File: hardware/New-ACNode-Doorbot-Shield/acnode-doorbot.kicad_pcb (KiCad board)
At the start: 2 copper layers, 55.9 x 124.5 mm, 19 parts, among them J1 Conn_02x10_Odd_Even, J10 Screw_Terminal_01x03, J2 Conn_02x10_Odd_Even, J3 Screw_Terminal_01x02, J4 Conn_02x10_Odd_Even, J5 Conn_02x10_Odd_Even, J6 Screw_Terminal_01x02, J7 Screw_Terminal_01x03, J8 RJ45, J9 Micro_SD_Card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

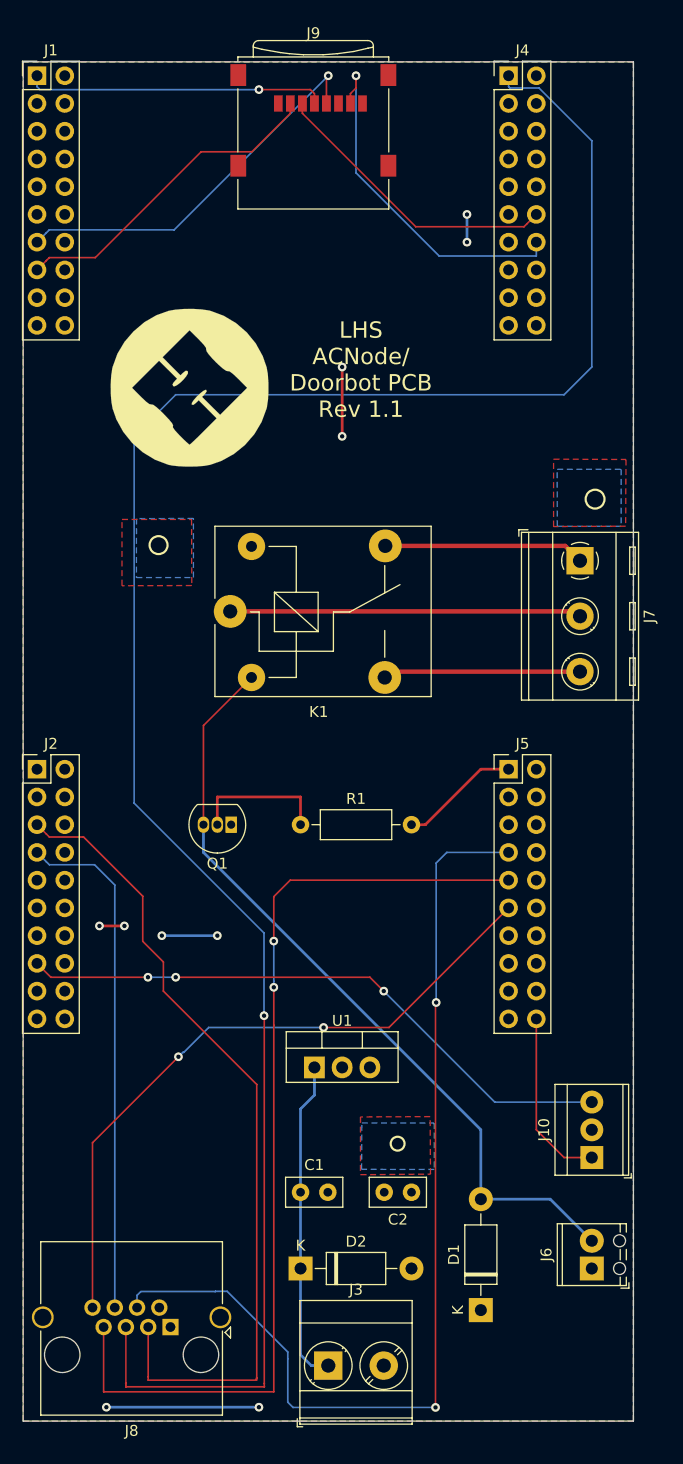
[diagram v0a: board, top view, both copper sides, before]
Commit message: some silkscreen documentation goodness
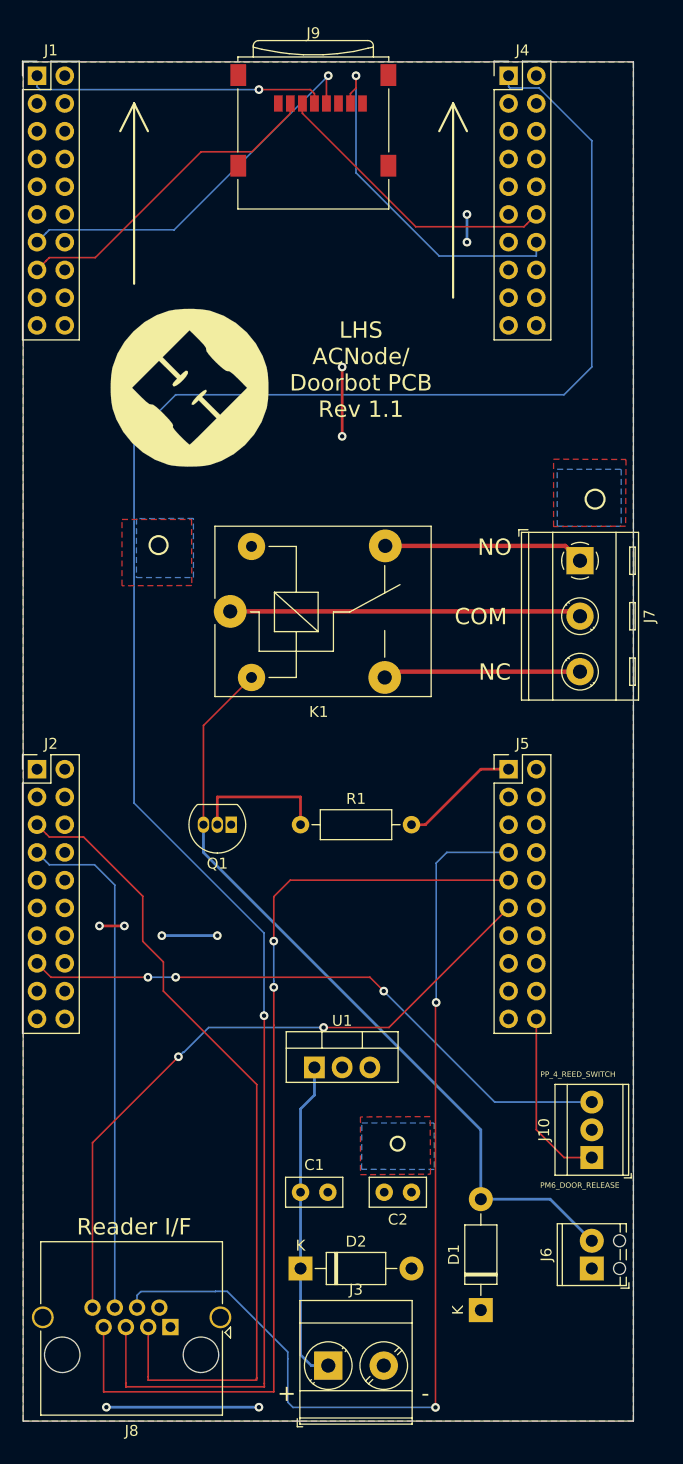
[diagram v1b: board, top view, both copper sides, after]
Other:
- board text added: "+"
- board text added: "-"
- board text added: "5-12V DC IN"
- board text added: "COM"
- board text added: "NC"
- board text added: "NO"
- board text added: "PM6_DOOR_RELEASE"
- board text added: "PP_4_REED_SWITCH"
- board text added: "Reader I/F"
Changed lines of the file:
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@@
-(kicad_pcb (version 20171130) (host pcbnew 5.0.1)
+(kicad_pcb (version 20171130) (host pcbnew "(5.0.1-3-g963ef8bb5)")
   (general
     (thickness 1.6)
-    (drawings 8)
+    (drawings 23)
     (tracks 169)
     (zones 0)
@@
   )
   (setup
-    (last_trace_width 0.1524)
+    (last_trace_width 0.25)
     (user_trace_width 0.1524)
     (user_trace_width 0.4064)
@@
     (solder_mask_min_width 0.25)
     (aux_axis_origin 0 0)
-    (visible_elements FFFFFF7F)
+    (visible_elements FFFFFFFF)
     (pcbplotparams
       (layerselection 0x010fc_ffffffff)
@@
       (xy 1.121055 -7.178742)) (layer F.SilkS) (width 0.01))
   )
+  (gr_line (start 90.17 44.45) (end 91.44 46.99) (layer F.SilkS) (width 0.2))
+  (gr_line (start 90.17 44.45) (end 88.9 46.99) (layer F.SilkS) (width 0.2))
+  (gr_line (start 90.17 62.23) (end 90.17 44.45) (layer F.SilkS) (width 0.2))
+  (gr_line (start 60.96 44.45) (end 62.23 46.99) (layer F.SilkS) (width 0.2))
+  (gr_line (start 60.96 44.45) (end 59.69 46.99) (layer F.SilkS) (width 0.2))
+  (gr_line (start 60.96 60.96) (end 60.96 44.45) (layer F.SilkS) (width 0.2))
+  (gr_text COM (at 92.71 91.44) (layer F.SilkS)
+    (effects (font (size 1.5 1.5) (thickness 0.3)))
+  )
+  (gr_text NO (at 93.98 85.09) (layer F.SilkS)
+    (effects (font (size 1.5 1.5) (thickness 0.3)))
+  )
+  (gr_text NC (at 93.98 96.52) (layer F.SilkS)
+    (effects (font (size 1.5 1.5) (thickness 0.3)))
+  )
+  (gr_text "Reader I/F" (at 60.96 147.32) (layer F.SilkS)
+    (effects (font (size 1.5 1.5) (thickness 0.3)))
+  )
+  (gr_text "5-12V DC IN" (at 81.28 153.67) (layer B.SilkS)
+    (effects (font (size 1 1) (thickness 0.25)) (justify mirror))
+  )
+  (gr_text - (at 87.63 162.56) (layer F.SilkS)
+    (effects (font (size 1.5 1.5) (thickness 0.3)))
+  )
+  (gr_text + (at 74.93 162.56) (layer F.SilkS)
+    (effects (font (size 1.5 1.5) (thickness 0.3)))
+  )
+  (gr_text PP_4_REED_SWITCH (at 101.6 133.35) (layer F.SilkS)
+    (effects (font (size 0.5 0.5) (thickness 0.125)))
+  )
+  (gr_text PM6_DOOR_RELEASE (at 105.41 143.51) (layer F.SilkS)
+    (effects (font (size 0.5 0.5) (thickness 0.125)) (justify right))
+  )
   (gr_circle (center 63.2 84.89) (end 63.82 85.43) (layer F.SilkS) (width 0.2))

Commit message: 1.1b of Dawid's design, some cosmetic changes only.
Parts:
- added ? (x2): , , F.Cu at (81.3, 113.0)
- moved G*** 3.17 mm to (66.0, 67.3)
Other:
- board text added: "+12V"
- board text added: "-GND"
- board text added: "LHS ACNode/ Doorbot PCB Rev 1.1a"
- board text added: "SRD-05VDC-SL-C"
- board text added: "Use long header pins"
- board text removed: "+"
- board text removed: "-"
- board text removed: "LHS ACNode/ Doorbot PCB Rev 1.1"

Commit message: slight tweaks I forgot to commit
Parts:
- removed the ? at (81.3, 113.0) (x2)
- added ? (x2): , , F.Cu at (81.3, 113.0)
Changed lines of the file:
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@@
     (pcbplotparams
       (layerselection 0x010fc_ffffffff)
-      (usegerberextensions false)
+      (usegerberextensions true)
       (usegerberattributes false)
       (usegerberadvancedattributes false)
@@
       (plotinvisibletext false)
       (padsonsilk false)
-      (subtractmaskfromsilk false)
+      (subtractmaskfromsilk true)
       (outputformat 1)
       (mirror false)

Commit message: Following feedback from Arthur, the rev 1.1a silkscreen was noted to be incorrect. Updating repo in case someone orders more boards.
Note errata in README.md
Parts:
- removed the ? at (81.3, 113.0) (x2)
- added ? (x2): , , F.Cu at (81.3, 113.0)
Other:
- board text added: "LHS ACNode/ Doorbot PCB Rev 1.1b"
- board text removed: "LHS ACNode/ Doorbot PCB Rev 1.1a"
